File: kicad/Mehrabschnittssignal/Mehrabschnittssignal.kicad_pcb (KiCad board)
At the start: 2 copper layers, 6.6 x 13.6 mm, 19 parts, among them J0 VCC, J1 VkzBw, J2 ROT, J3 GRÜN, J4 GELB, J5 Zs7-3, J6 Ra, J7 Zs7-1, J8 Zs7-2, J9 Ra/Zs1

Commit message: Update MS README
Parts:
- D3: value LED_Y -> LED_G
- D5: value LED_G -> LED_Y
- J3: value GRÜN -> GELB
- J4: value GELB -> GRÜN

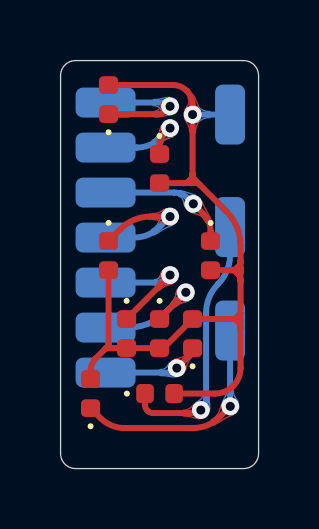
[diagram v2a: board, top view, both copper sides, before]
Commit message: MS: keep more space to border for breakout
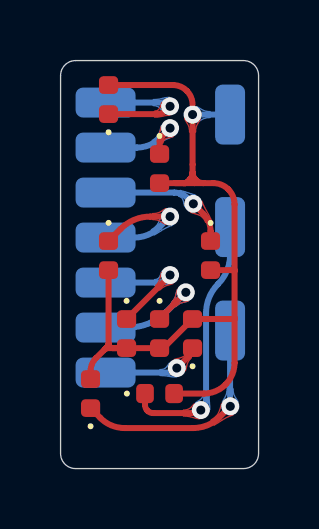
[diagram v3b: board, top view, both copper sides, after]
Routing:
- net Net-(D1-Pad2): track 30.8 -> 28.7 mm
- net Net-(D7-Pad1): track 4.33 -> 3.55 mm
